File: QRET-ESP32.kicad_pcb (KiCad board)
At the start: 4 copper layers, 123.9 x 86.3 mm, 126 parts, among them J1 Conn_01x04, J10 Conn_01x04, J2 Conn_01x02, J3 Conn_02x01, J4 Conn_01x02, J5 Conn_01x02, J6 Conn_01x02, J7 Conn_02x04_Counter_Clockwise, J8 Conn_02x04_Counter_Clockwise, J9 Conn_01x04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

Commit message: Placed the general sets of components.
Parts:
- moved C5 99.7 mm to (50.1, 142.5)
- moved C6 97.5 mm to (58.9, 140.5)
- moved F1 97.1 mm to (29.6, 131.5)
- moved D2 96.9 mm to (39.5, 142.5)
- moved J3 96.7 mm to (29.5, 139.8)
- moved C21 88.7 mm to (158.9, 141.3)
- moved C10 88.6 mm to (128.3, 139.3), turned to -90 degrees
- moved C12 88.6 mm to (131.8, 139.3), turned to -90 degrees
- moved U4 88.3 mm to (138.0, 139.3)
- moved R16 87.8 mm to (132.3, 141.9)
- moved C19 87.3 mm to (156.1, 141.3)
- moved C14 87.0 mm to (142.9, 139.4), turned to -90 degrees
- moved C15 86.8 mm to (143.7, 136.3), turned to 90 degrees
- moved R10 86.1 mm to (139.7, 171.5), turned to -90 degrees
- moved C18 85.8 mm to (152.8, 141.3)
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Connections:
- R22 pad 1: Heat_1_Current -> Load_Cell+
- R24 pad 1: Load_Cell+ -> Heat_1_Current
- U1 pad 14: A1_Control -> Nitrous_Control
- U1 pad 15: A2_Control -> 24V_GOOD
- U1 pad 16: Nitrous_Control -> 12V_GOOD
- U1 pad 6: 24V_GOOD -> A1_Control
- U1 pad 7: 12V_GOOD -> A2_Control
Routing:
- net GND: track 354.5 -> 0.00 mm, vias 40 -> 0
- net +3.3V: track 212.4 -> 0.00 mm, vias 20 -> 0
- net +24V: track 191.5 -> 0.00 mm, vias 14 -> 0
- net +5V: track 159.0 -> 0.00 mm, vias 20 -> 0
- net /Power_Regulation/+5.3V: track 144.9 -> 0.00 mm, vias 4 -> 0
- net /Power_Regulation/+5V_EN: track 100.4 -> 0.00 mm, vias 4 -> 0
- net /Power_Regulation/+3.3V_EN: track 91.4 -> 0.00 mm, vias 4 -> 0
- net +12V: track 88.0 -> 0.00 mm, vias 5 -> 0
- net I2C_Clock: track 76.3 -> 0.00 mm
- net I2C_Data: track 64.2 -> 0.00 mm, vias 2 -> 0
- net Nitrous_Control: track 56.0 -> 0.00 mm, vias 2 -> 0
- net Fan_2_PWM: track 55.1 -> 0.00 mm
- net Fan_2_Control: track 55.1 -> 0.00 mm
- net Fan_1_Control: track 53.7 -> 0.00 mm
- net Fan_1_PWM: track 53.2 -> 0.00 mm
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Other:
- board outline removed
- board text removed: "Ground Support Equipment ESP32 Board Version 1"
- board text removed: "I'm sure this all sucks. 3.3EN and PWR-SQ are particularly bad here."

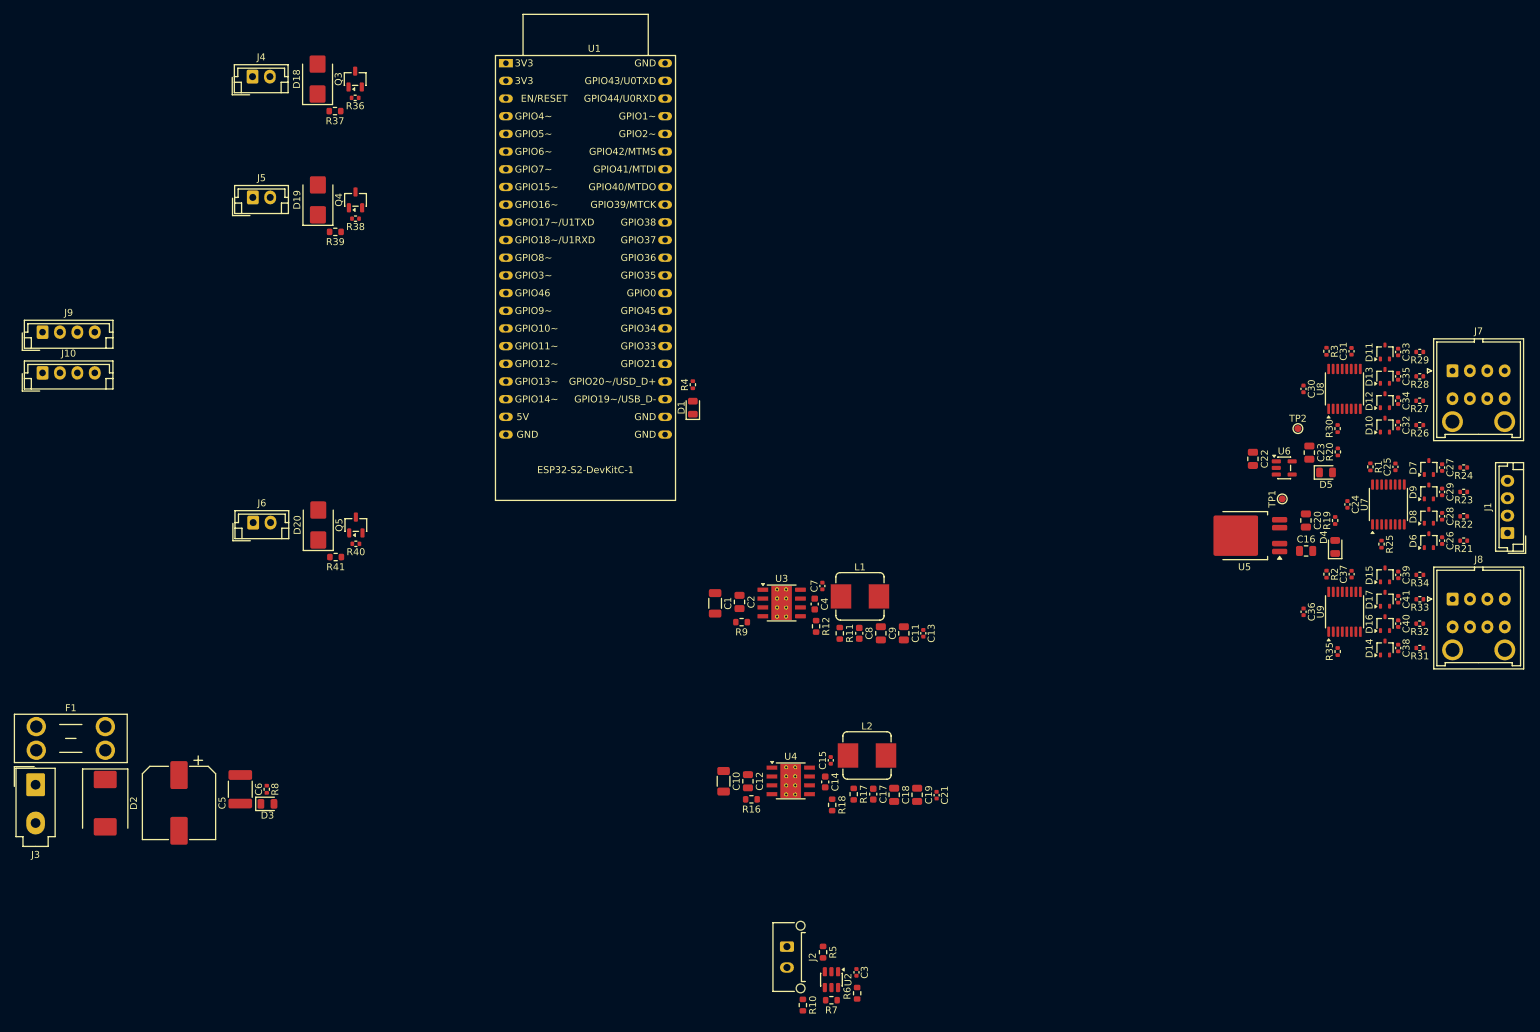
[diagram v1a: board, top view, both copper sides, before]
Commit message: General board shape, mounting holes, grounding plates.
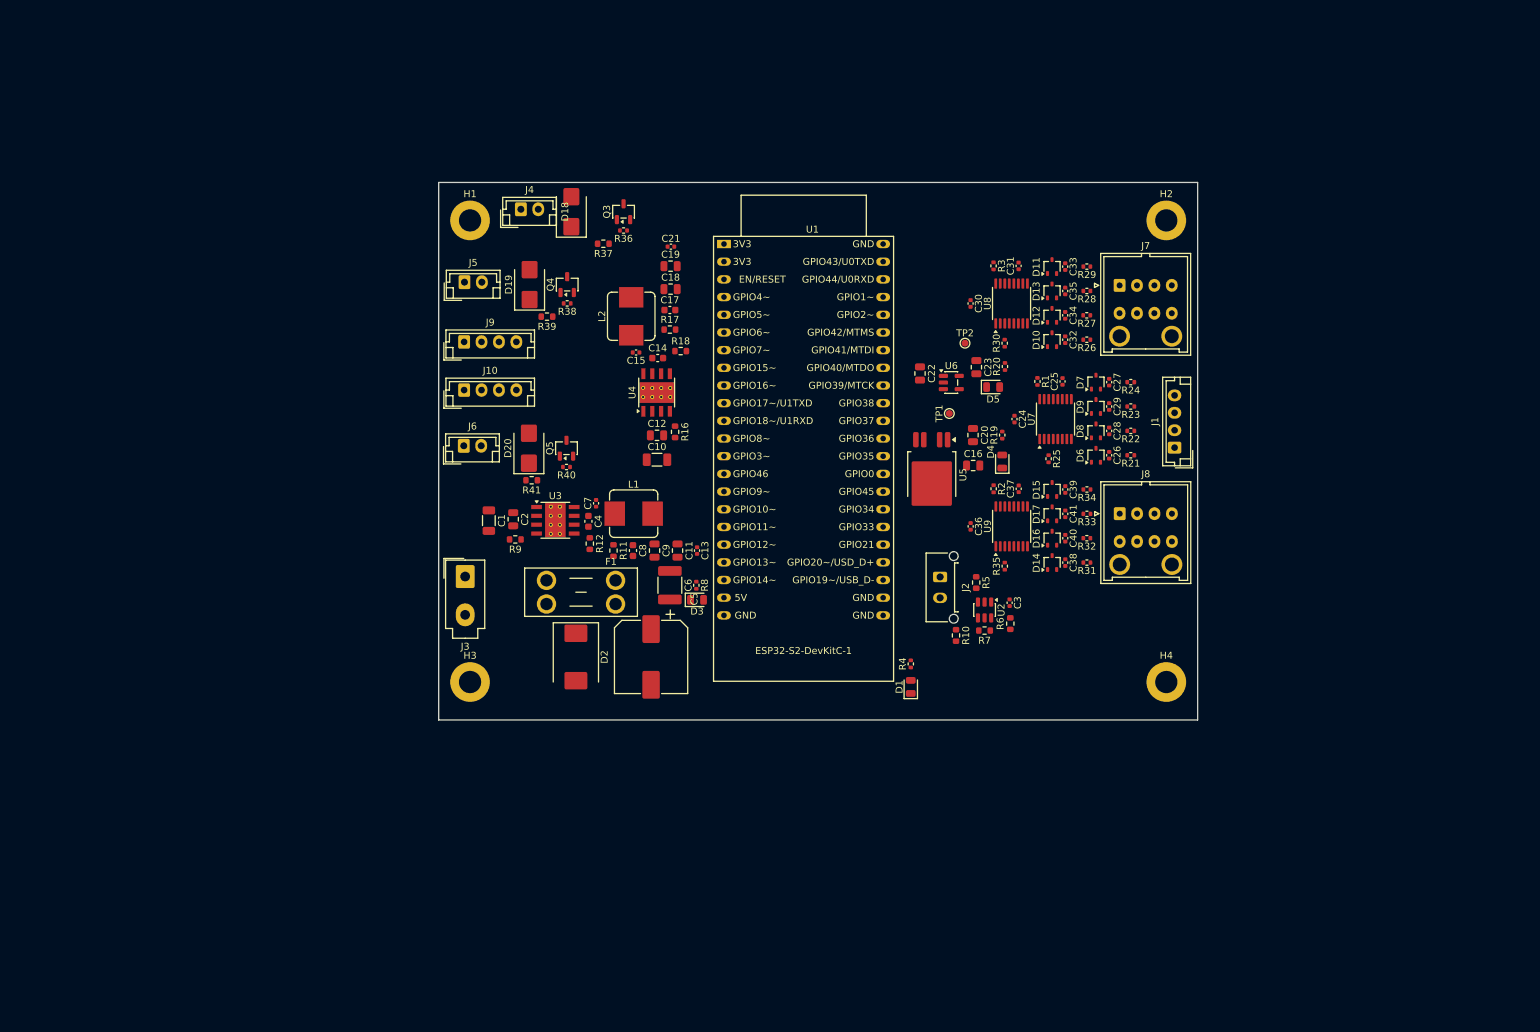
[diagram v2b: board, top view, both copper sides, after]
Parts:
- added H1: MountingHole_Pad, MountingHole:MountingHole_3.2mm_M3_ISO7380_Pad, F.Cu at (91.9, 58.8)
- added H2: MountingHole_Pad, MountingHole:MountingHole_3.2mm_M3_ISO7380_Pad, F.Cu at (191.9, 58.8)
- added H3: MountingHole_Pad, MountingHole:MountingHole_3.2mm_M3_ISO7380_Pad, F.Cu at (91.9, 125.1)
- added H4: MountingHole_Pad, MountingHole:MountingHole_3.2mm_M3_ISO7380_Pad, F.Cu at (191.9, 125.1)
- moved C21 87.5 mm to (120.8, 62.6), turned to 180 degrees
- moved C19 83.8 mm to (120.7, 65.4), turned to 0 degrees
- moved C18 79.4 mm to (120.7, 68.7), turned to 0 degrees
- moved F1 76.2 mm to (102.9, 110.5)
- moved C17 75.4 mm to (120.6, 71.7), turned to 0 degrees
- moved R17 71.8 mm to (120.6, 74.5), turned to 0 degrees
- moved L2 71.6 mm to (115.0, 72.6), turned to 90 degrees
- moved C5 71.0 mm to (117.9, 121.5)
- moved D2 70.8 mm to (107.1, 121.5)
- moved R18 68.7 mm to (122.2, 77.6), turned to 0 degrees
- moved J3 68.6 mm to (91.2, 110.0)
- moved D3 68.3 mm to (124.5, 113.3)
- moved R8 68.3 mm to (124.4, 111.2)
- moved C6 68.3 mm to (120.6, 111.2)
- moved C14 65.5 mm to (118.8, 78.6), turned to 0 degrees
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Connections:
- U1 pad 28: I2C_Clock -> I2C_Data
- U1 pad 29: I2C_Data -> I2C_Clock
- U1 pad 4: Fan_1_Control -> A1_Control
- U1 pad 5: Fan_1_PWM -> A2_Control
- U1 pad 6: A1_Control -> Fan_1_Control
- U1 pad 7: A2_Control -> Fan_1_PWM
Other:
- board outline added: 109 x 77.2 mm

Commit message: Second draft of placement and wiring.
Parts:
- moved D1 61.5 mm to (159.8, 64.5), turned to 180 degrees
- moved R4 58.0 mm to (156.5, 64.5), turned to 180 degrees
- moved C13 30.6 mm to (94.6, 99.8)
- moved C1 30.2 mm to (124.6, 105.5), turned to 90 degrees
- moved C9 26.4 mm to (92.8, 99.7), turned to 90 degrees
- moved C11 25.2 mm to (97.4, 99.7)
- moved C2 23.4 mm to (121.1, 105.8), turned to 90 degrees
- moved R9 23.3 mm to (121.3, 100.4), turned to 0 degrees
- moved C8 13.7 mm to (104.1, 98.3), turned to 90 degrees
- moved L1 12.1 mm to (103.6, 103.4), turned to 180 degrees
- moved U3 10.7 mm to (114.8, 102.5), turned to 180 degrees
- moved R11 9.72 mm to (107.0, 98.2), turned to 90 degrees
- moved R12 6.17 mm to (109.9, 99.1), turned to 90 degrees
- moved C7 5.55 mm to (109.0, 104.9), turned to -90 degrees
- moved R2 5.13 mm to (171.3, 94.4)
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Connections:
- J10 pad 1: +12V -> GND
- J10 pad 2: Fan_2_Control -> +12V
- J10 pad 3: Fan_2_PWM -> Fan_2_Control
- J10 pad 4: GND -> Fan_2_PWM
- J7 pad 1: Heat_1_Power -> +3.3V
- J8 pad 1: Heat_2_Power -> +3.3V
- J9 pad 1: +12V -> GND
- J9 pad 2: Fan_1_Control -> +12V
- J9 pad 3: Fan_1_PWM -> Fan_1_Control
- J9 pad 4: GND -> Fan_1_PWM
- U1 pad 27: /ESP32-Breakout/WIFI_IND -> unconnected-(U1-GPIO21-Pad27)
- U1 pad 30: unconnected-(U1-GPIO45-Pad30) -> DRDY3
- U1 pad 34: unconnected-(U1-GPIO37-Pad34) -> DRDY1
- U1 pad 37: DRDY3 -> unconnected-(U1-GPIO40/MTDO-Pad37)
- U1 pad 38: DRDY2 -> unconnected-(U1-GPIO41/MTDI-Pad38)
- U1 pad 39: DRDY1 -> DRDY2
- U1 pad 43: unconnected-(U1-GPIO43/U0TXD-Pad43) -> /ESP32-Breakout/WIFI_IND
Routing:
- net +3.3V: track 0.00 -> 204.8 mm, vias 0 -> 20
- net +24V: track 0.00 -> 154.0 mm, vias 0 -> 9
- net GND: track 0.00 -> 139.3 mm, vias 0 -> 120
- net /Power_Regulation/+5.3V: track 0.00 -> 132.8 mm, vias 0 -> 6
- net +5V: track 0.00 -> 126.2 mm, vias 0 -> 18
- net I2C_Clock: track 0.00 -> 62.4 mm, vias 0 -> 2
- net I2C_Data: track 0.00 -> 56.7 mm
- net /Power_Regulation/+12_EN: track 0.00 -> 54.5 mm, vias 0 -> 2
- net +12V: track 0.00 -> 46.9 mm, vias 0 -> 1
- net /Power_Regulation/+5V_EN: track 0.00 -> 46.7 mm, vias 0 -> 2
- net /Power_Regulation/+3.3V_EN: track 0.00 -> 39.6 mm, vias 0 -> 2
- net Fan_2_Control: track 0.00 -> 33.7 mm, vias 0 -> 2
- net Fan_1_Control: track 0.00 -> 31.7 mm, vias 0 -> 2
- net Fan_2_PWM: track 0.00 -> 31.2 mm, vias 0 -> 2
- net DRDY1: track 0.00 -> 30.4 mm, vias 0 -> 2
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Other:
- board size 109 x 77.2 mm -> 111.5 x 77 mm

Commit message: Added labels and notes.
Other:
- board text added: "12V Step-Down"
- board text added: "24V Input"
- board text added: "24V ON"
- board text added: "3.3V Regulation"
- board text added: "5.3V Step-Down"
- board text added: "5V Regulation"
- board text added: "Actuator 1"
- board text added: "Actuator 2"
- board text added: "Fans 1&2"
- board text added: "Ground Support Equipment PCB Draft 2 2026-04-07"
- board text added: "Heating Control System 1"
- board text added: "Heating Control System 2"
- board text added: "Load Cell"
- board text added: "Nitrous Actuator"
- board text added: "Notes pre-review: Is there a better place to put Power Sequencing? This one puts it close to 3.3V and 5V, but not 12V. Is there a better way to place things to avoid snaking lines over/under eachother? Are the sockets too close to eachother to be practically soldered/used? Should I be worried about capacitance of the 2 inner plates in the zones devoid of GND vias?"
- board text added: "Power Sequencing"
- board text added: "WIFI ON"
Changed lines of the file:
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@@
 		(layer "Edge.Cuts")
+	)
+	(gr_text "Ground Support Equipment PCB\nDraft 2\n2026-04-07"
+		(at 187.5 127 0)
+		(layer "F.SilkS")
+		(effects
+			(font
+				(size 1 1)
+				(thickness 0.1)
+			)
+			(justify right bottom)
+		)
+	)
+	(gr_text "12V Step-Down"
+		(at 111.6 98.4 0)
+		(layer "F.SilkS")
+		(effects
+			(font
+				(size 0.6 0.6)
+				(thickness 0.1)
+			)
+			(justify left bottom)
+		)
+	)
+	(gr_text "Actuator 2"
+		(at 97.4 64.29 0)
+		(layer "F.SilkS")
+		(effects
+			(font
+				(size 0.6 0.6)
+				(thickness 0.1)
+			)
+			(justify left bottom)
+		)
+	)
+	(gr_text "Load Cell"
+		(at 191.1 80.5 0)
+		(layer "F.SilkS")
+		(effects
+			(font
+				(size 0.6 0.6)
+				(thickness 0.1)
+			)
+			(justify left bottom)
+		)
+	)
+	(gr_text "Heating Control System 1"
+		(at 172.5 62.4 0)
+		(layer "F.SilkS")
+		(effects
+			(font
+				(size 0.6 0.6)
+				(thickness 0.1)
+			)
+			(justify left bottom)
+		)
+	)
+	(gr_text "Power Sequencing"
+		(at 157.3 120.9 0)
+		(layer "F.SilkS")
+		(effects
+			(font
+				(size 0.6 0.6)
+				(thickness 0.1)
+			)
+			(justify left bottom)
+		)
+	)
+	(gr_text "Nitrous Actuator"
+		(at 96.1 87.7 0)
+		(layer "F.SilkS")
+		(effects
+			(font
+				(size 0.6 0.6)
+				(thickness 0.1)
+			)
+			(justify left bottom)
+		)
+	)
+	(gr_text "5.3V Step-Down"
+		(at 109.4 67 0)
+		(layer "F.SilkS")
+		(effects
+			(font
+				(size 0.6 0.6)
+				(thickness 0.1)
+			)
+			(justify left bottom)
+		)
+	)
+	(gr_text "Heating Control System 2"
+		(at 180 113.2 0)
+		(layer "F.SilkS")
+		(effects
+			(font
+				(size 0.6 0.6)
+				(thickness 0.1)
+			)
+			(justify left bottom)
+		)
+	)
+	(gr_text "3.3V Regulation"
+		(at 153.5 104 0)
+		(layer "F.SilkS")
+		(effects
+			(font
+				(size 0.6 0.6)
+				(thickness 0.1)
+			)
+			(justify left bottom)
+		)
+	)
+	(gr_text "5V Regulation"
+		(at 155.6 78 0)
+		(layer "F.SilkS")
+		(effects
+			(font
+				(size 0.6 0.6)
+				(thickness 0.1)
+			)
+			(justify left bottom)
+		)
+	)
+	(gr_text "Fans 1&2"
+		(at 101.8 80.5 0)
+		(layer "F.SilkS")
+		(effects
+			(font
+				(size 0.6 0.6)
+				(thickness 0.1)
+			)
+			(justify left bottom)
+		)
+	)
+	(gr_text "WIFI ON"
+		(at 159.8 62.6 0)
+		(layer "F.SilkS")
+		(effects
+			(font
+				(size 0.8 0.8)
+				(thickness 0.16)
+				(bold yes)
+			)
+			(justify bottom)
+		)
+	)
+	(gr_text "Notes pre-review:\nIs there a better place to put Power Sequencing?\nThis one puts it close to 3.3V and 5V, but not 12V.\n\nIs there a better way to place things to avoid snaking lines over/under eachother?\n\nAre the sockets too close to eachother to be practically soldered/used?\n\nShould I be worried about capacitance of the 2 inner plates in the zones devoid of GND vias?\n"
+		(at 88.4 148.1 0)
+		(layer "F.SilkS")
+		(effects
+			(font
+				(size 1 1)
+				(thickness 0.1)
+			)
+			(justify left bottom)
+		)
+	)
+	(gr_text "24V ON"
+		(at 125.8 120.5 90)
+		(layer "F.SilkS")
+		(effects
+			(font
+				(size 0.8 0.8)
+				(thickness 0.2)
+				(bold yes)
+			)
+			(justify left bottom)
+		)
+	)
+	(gr_text "24V Input"
+		(at 95.7 121.9 0)
+		(layer "F.SilkS")
+		(effects
+			(font
+				(size 1 1)
+				(thickness 0.1)
+			)
+			(justify left bottom)
+		)
+	)
+	(gr_text "Actuator 1"
+		(at 99.6 61.7 0)
+		(layer "F.SilkS")
+		(effects
+			(font
+				(size 0.6 0.6)
+				(thickness 0.1)
+			)
+			(justify left bottom)
+		)
 	)
 	(segment
